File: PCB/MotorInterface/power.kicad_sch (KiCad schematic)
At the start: 2 parts, among them U2 74LS14, U3 74LS08

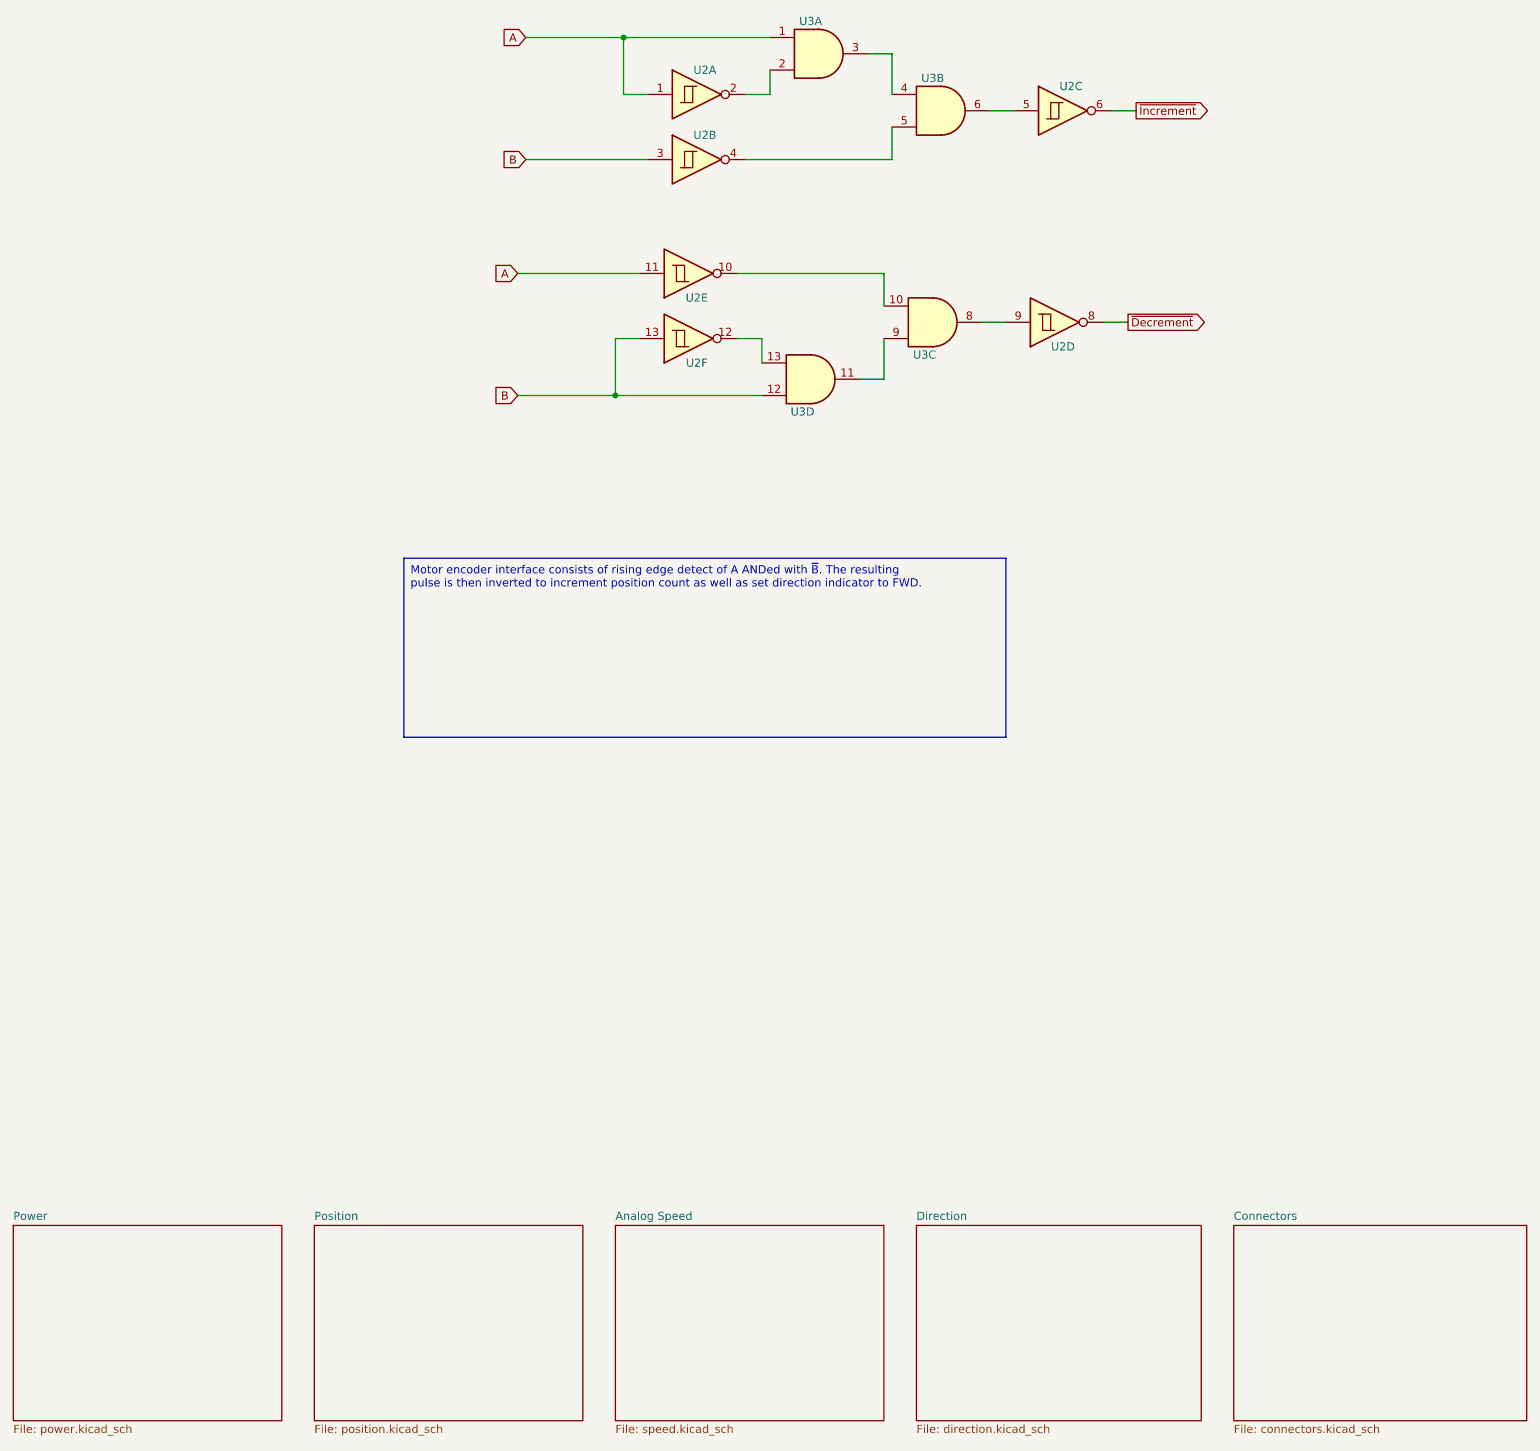
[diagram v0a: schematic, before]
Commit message: split schema into sheets
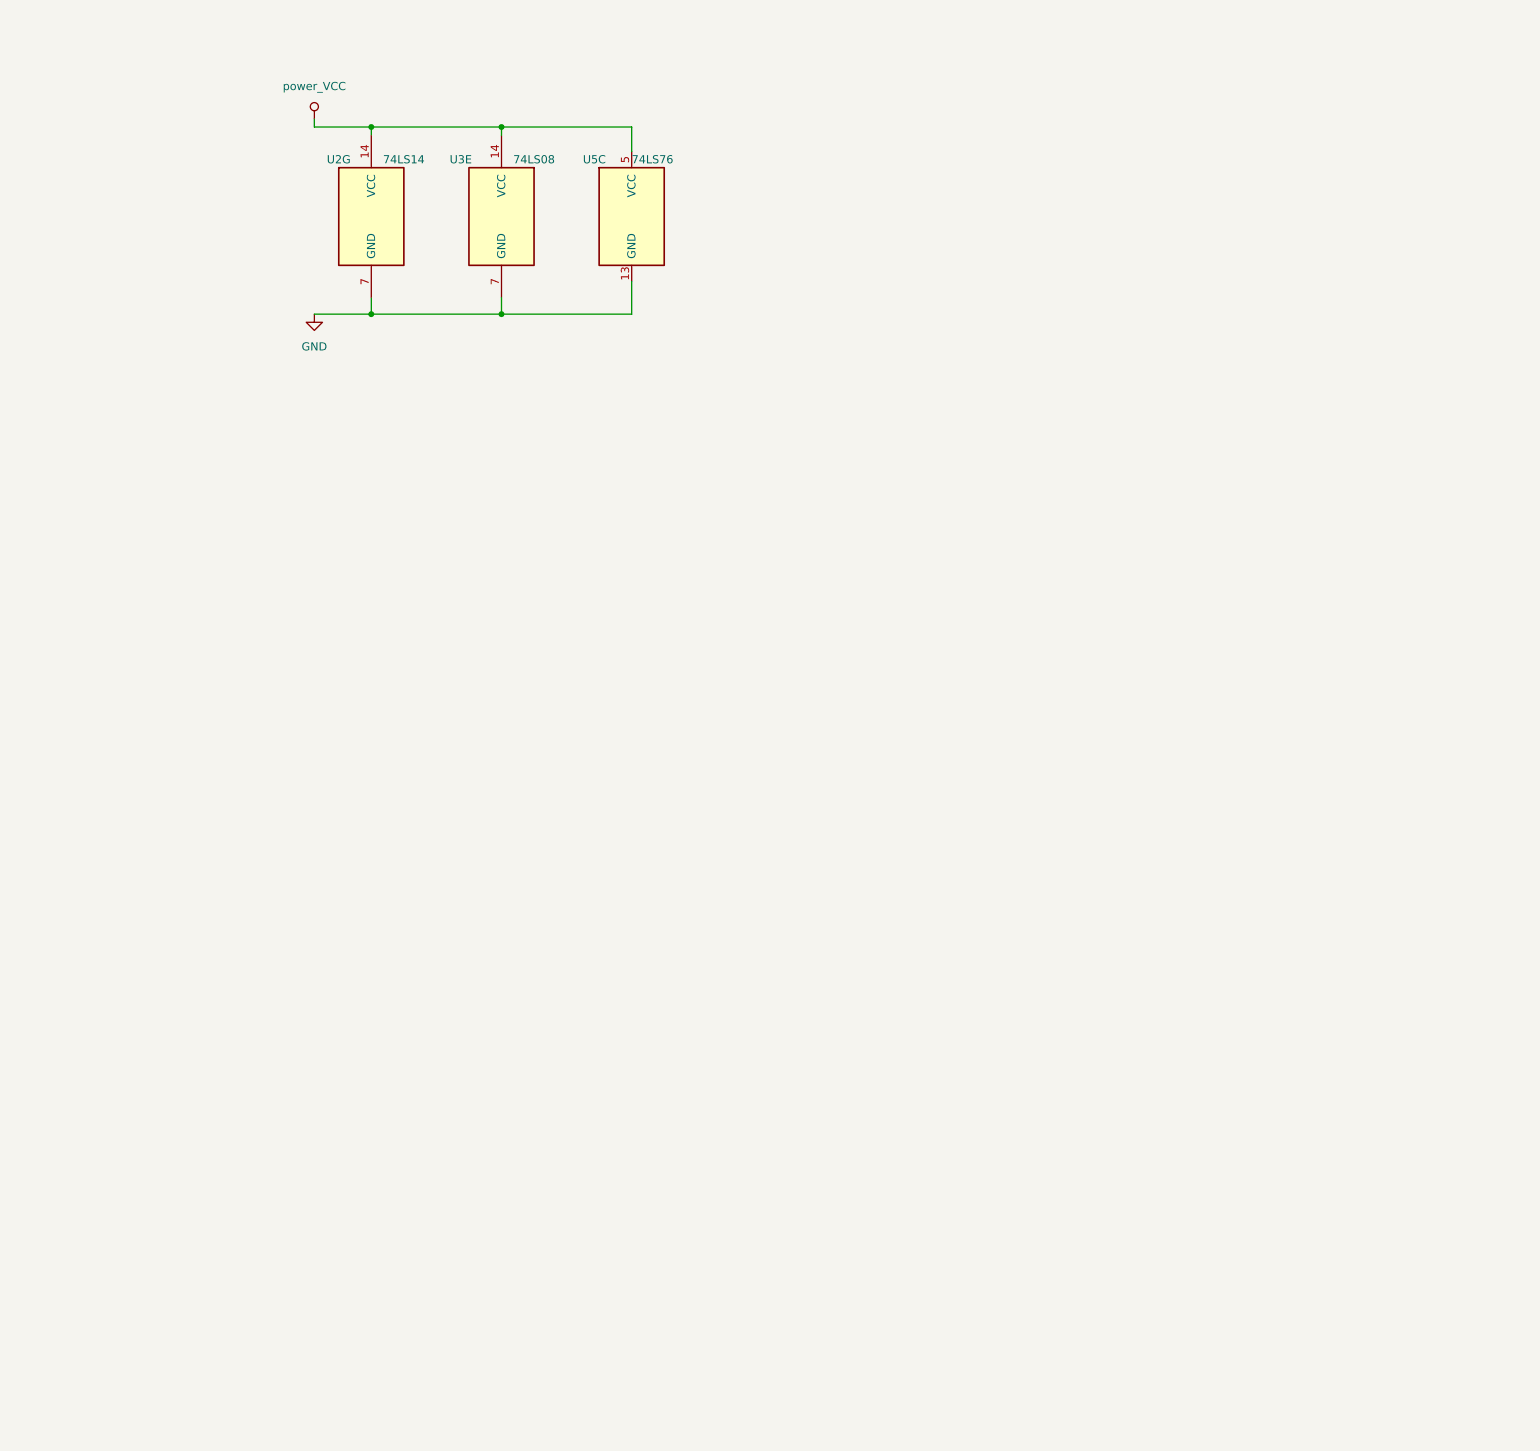
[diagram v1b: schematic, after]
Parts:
- removed U2: 74LS14, symbol S2020-cache:74xx_74LS14
- removed U3: 74LS08, symbol TFlipFlop-cache:74xx_74LS08
- added U2: 74LS14, symbol S2020-cache:74xx_74LS14
- added U3: 74LS08, symbol TFlipFlop-cache:74xx_74LS08
- added U5: 74LS76, symbol 00TJR:74xx_74LS76
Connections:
- new net GND: U2.7 (GND), U3.7 (GND), U5.13 (GND)
- new net VCC: U2.14 (VCC), U3.14 (VCC), U5.5 (VCC)
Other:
- removed sheet Analog Speed
- removed sheet Connectors
- removed sheet Direction
- removed sheet Position
- removed sheet Power
